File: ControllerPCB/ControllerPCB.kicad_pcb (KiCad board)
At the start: 2 copper layers, 88 parts, among them J1 2x20 Conn_1, J10 Conn_01x03_Pin, J11 1x4 String Output Conn, J12 2x4 Pickup Conn, J13 9V Humbucker OUT, J14 9V IN, J15 MIDI Out Conn, J2 Conn_01x03_Pin, J3 Conn_01x03_Pin, J4 10-pin Debug Conn, J5 Conn_01x03_Pin, J6 Conn_01x03_Pin, J7 USB_B_Micro, J8 2x20 Conn_2, J9 Conn_01x03_Pin, SW1 SW_SPDT, U1 STM32F439ZIT6, U2 ADP3336ARMZ, U3 74LVC1G17, Y1 8MHz

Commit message: rev 0.3
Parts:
- removed D1: D+_TVS, PESD3V6Z1BCSFYL:PMEG3005AESFYL
- removed D10, D11, D12, D13, D14, D15, D16, D17, D6, D7, D8, D9: MBR0520LT, Diode_SMD:D_SOD-123
- removed D2: VBUS_TVS, PESD5V5C1BLYL:PESD5V5C1BLYL
- removed D3: D-_TVS, PESD3V6Z1BCSFYL:PMEG3005AESFYL
- removed D4: TVS_Bat, TPSMB10CA:DIONM5436X244N
- removed J1: 2x20 Conn_1, 75869-107LF:SHDR40W62P254_2X20_5801X920X957P
- removed J10: Conn_01x03_Pin, 22292031:CONN_AE-6410-03A_MOL
- removed J11: 1x4 String Output Conn, 22292041:CONN_AE-6410-04A_MOL
- removed J8: 2x20 Conn_2, 75869-107LF:SHDR40W62P254_2X20_5801X920X957P
- removed R11, R18, R19: 5k, Resistor_SMD:R_0402_1005Metric
- removed R14, R20, R22: 1k, Resistor_SMD:R_0402_1005Metric
- removed R15, R21, R23: 10k, Resistor_SMD:R_0402_1005Metric
- removed R16, R17, R24, R25: 2k, Resistor_SMD:R_0402_1005Metric
- removed SW1: SW_SPDT, JS102011SAQN:SW_JS102011SAQN
- added C401: 10n, Capacitor_SMD:C_0402_1005Metric, F.Cu at (111.2, 137.2)
- added C402: 10n, Capacitor_SMD:C_0402_1005Metric, F.Cu at (117.0, 137.2)
- added C403: 10n, Capacitor_SMD:C_0402_1005Metric, F.Cu at (128.4, 137.2)
- added C404: 10n, Capacitor_SMD:C_0402_1005Metric, F.Cu at (122.7, 137.2)
- added D101: BLUE, LED_SMD:LED_0603_1608Metric, F.Cu at (128.3, 67.2)
- added D102: D_TVS_Small, 0_Footprint_lib:PMEG3005AESFYL, F.Cu at (163.9, 93.3)
- added D103: D_TVS_Small, 0_Footprint_lib:PMEG3005AESFYL, F.Cu at (191.0, 126.3)
- added D104: D_TVS_Small, 0_Footprint_lib:PMEG3005AESFYL, F.Cu at (163.9, 95.2)
- added D105: D_TVS_Small, 0_Footprint_lib:PMEG3005AESFYL, F.Cu at (126.0, 89.3)
- added D106: D_TVS_Small, 0_Footprint_lib:PMEG3005AESFYL, F.Cu at (128.5, 89.3)
- added D107: D_TVS_Small, 0_Footprint_lib:PMEG3005AESFYL, F.Cu at (163.9, 97.3)
- added D108: D_TVS_Small, 0_Footprint_lib:PMEG3005AESFYL, F.Cu at (192.0, 127.4)
- added D109: D_TVS_Small, 0_Footprint_lib:PMEG3005AESFYL, F.Cu at (192.0, 130.3)
- added D110: D_TVS_Small, 0_Footprint_lib:PMEG3005AESFYL, F.Cu at (131.2, 89.3)
- added D111: D_TVS_Small, 0_Footprint_lib:PMEG3005AESFYL, F.Cu at (163.9, 99.3)
- added D112: D_TVS_Small, 0_Footprint_lib:PMEG3005AESFYL, F.Cu at (133.7, 89.3)
- added D113: D_Small, Diode_SMD:D_SOD-323, F.Cu at (134.0, 91.6)
- added D114: D_Small, Diode_SMD:D_SOD-323, F.Cu at (131.5, 91.6)
- added D115: D_Small, Diode_SMD:D_SOD-323, F.Cu at (128.9, 91.6)
- added D116: D_Small, Diode_SMD:D_SOD-323, F.Cu at (126.4, 91.6)
- added D117: D_TVS_Small, 0_Footprint_lib:PMEG3005AESFYL, F.Cu at (169.2, 100.0)
- added D201: D_TVS_Small, 0_Footprint_lib:PMEG3005AESFYL, F.Cu at (151.8, 89.2)
- added D401: D_Small, Diode_SMD:D_SOD-323, F.Cu at (122.2, 132.7)
- added D402: D_Small, Diode_SMD:D_SOD-323, F.Cu at (122.2, 134.7)
- added D403: D_Small, Diode_SMD:D_SOD-323, F.Cu at (110.7, 132.7)
- added D404: D_Small, Diode_SMD:D_SOD-323, F.Cu at (110.7, 134.7)
- added D405: D_Small, Diode_SMD:D_SOD-323, F.Cu at (122.2, 130.7)
- added D406: D_Small, Diode_SMD:D_SOD-323, F.Cu at (110.7, 130.7)
- added D407: D_Small, Diode_SMD:D_SOD-323, F.Cu at (128.0, 132.7)
- added D408: D_Small, Diode_SMD:D_SOD-323, F.Cu at (128.0, 134.7)
- added D409: D_Small, Diode_SMD:D_SOD-323, F.Cu at (116.5, 132.7)
- added D410: D_Small, Diode_SMD:D_SOD-323, F.Cu at (116.5, 134.7)
- added D411: D_Small, Diode_SMD:D_SOD-323, F.Cu at (128.0, 130.7)
- added D412: D_Small, Diode_SMD:D_SOD-323, F.Cu at (116.5, 130.7)
- added D501: D_TVS_Small, 0_Footprint_lib:PMEG3005AESFYL, B.Cu at (193.7, 63.8)
- added D502: D_TVS_Small, 0_Footprint_lib:PMEG3005AESFYL, B.Cu at (193.7, 66.3)
- added D503: D_TVS_Small, 0_Footprint_lib:PMEG3005AESFYL, B.Cu at (193.7, 68.8)
- added D504: D_TVS_Small, 0_Footprint_lib:PMEG3005AESFYL, B.Cu at (193.7, 71.3)
- added D505: D_TVS_Small, 0_Footprint_lib:PMEG3005AESFYL, B.Cu at (193.7, 74.1)
- added D506: D_TVS_Small, 0_Footprint_lib:PMEG3005AESFYL, B.Cu at (193.8, 76.6)
- added D507: D_TVS_Small, 0_Footprint_lib:PMEG3005AESFYL, B.Cu at (193.8, 79.1)
- added D508: D_TVS_Small, 0_Footprint_lib:PMEG3005AESFYL, B.Cu at (193.7, 81.3)
- added D509: D_TVS_Small, 0_Footprint_lib:PMEG3005AESFYL, B.Cu at (193.7, 83.8)
- added D510: D_TVS_Small, 0_Footprint_lib:PMEG3005AESFYL, B.Cu at (193.7, 86.6)
- added D511: D_TVS_Small, 0_Footprint_lib:PMEG3005AESFYL, B.Cu at (193.8, 89.3)
- added D512: D_TVS_Small, 0_Footprint_lib:PMEG3005AESFYL, B.Cu at (193.7, 92.1)
- added D513: D_TVS_Small, 0_Footprint_lib:PMEG3005AESFYL, B.Cu at (193.8, 94.6)
- added D514: D_TVS_Small, 0_Footprint_lib:PMEG3005AESFYL, B.Cu at (193.7, 97.1)
- added D515: D_TVS_Small, 0_Footprint_lib:PMEG3005AESFYL, B.Cu at (193.7, 99.6)
- added D516: D_TVS_Small, 0_Footprint_lib:PMEG3005AESFYL, B.Cu at (193.7, 102.1)
- added D517: D_TVS_Small, 0_Footprint_lib:PMEG3005AESFYL, B.Cu at (193.8, 104.8)
- added D518: D_TVS_Small, 0_Footprint_lib:PMEG3005AESFYL, B.Cu at (193.8, 107.6)
- added D519: D_TVS_Small, 0_Footprint_lib:PMEG3005AESFYL, B.Cu at (193.7, 110.1)
- added D520: D_TVS_Small, 0_Footprint_lib:PMEG3005AESFYL, B.Cu at (193.8, 112.8)
- added D521: D_TVS_Small, 0_Footprint_lib:PMEG3005AESFYL, B.Cu at (181.4, 64.1)
- added D522: D_TVS_Small, 0_Footprint_lib:PMEG3005AESFYL, B.Cu at (181.4, 66.6)
- added D523: D_TVS_Small, 0_Footprint_lib:PMEG3005AESFYL, B.Cu at (181.4, 69.1)
- added D524: D_TVS_Small, 0_Footprint_lib:PMEG3005AESFYL, B.Cu at (181.4, 71.6)
- added D525: D_TVS_Small, 0_Footprint_lib:PMEG3005AESFYL, B.Cu at (181.4, 74.1)
- added D526: D_TVS_Small, 0_Footprint_lib:PMEG3005AESFYL, B.Cu at (181.4, 76.6)
- added D527: D_TVS_Small, 0_Footprint_lib:PMEG3005AESFYL, B.Cu at (181.4, 79.3)
- added D528: D_TVS_Small, 0_Footprint_lib:PMEG3005AESFYL, B.Cu at (181.4, 81.8)
- added D529: D_TVS_Small, 0_Footprint_lib:PMEG3005AESFYL, B.Cu at (181.4, 84.3)
- added D530: D_TVS_Small, 0_Footprint_lib:PMEG3005AESFYL, B.Cu at (181.4, 86.8)
- added D531: D_TVS_Small, 0_Footprint_lib:PMEG3005AESFYL, B.Cu at (181.4, 89.3)
- added D532: D_TVS_Small, 0_Footprint_lib:PMEG3005AESFYL, B.Cu at (181.4, 91.8)
- added D533: D_TVS_Small, 0_Footprint_lib:PMEG3005AESFYL, B.Cu at (181.4, 94.3)
- added D534: D_TVS_Small, 0_Footprint_lib:PMEG3005AESFYL, B.Cu at (181.4, 96.8)
- added D535: D_TVS_Small, 0_Footprint_lib:PMEG3005AESFYL, B.Cu at (181.4, 99.3)
- added D536: D_TVS_Small, 0_Footprint_lib:PMEG3005AESFYL, B.Cu at (181.4, 101.8)
- added D537: D_TVS_Small, 0_Footprint_lib:PMEG3005AESFYL, B.Cu at (181.4, 104.8)
- added D538: D_TVS_Small, 0_Footprint_lib:PMEG3005AESFYL, B.Cu at (181.4, 107.3)
- added D539: D_TVS_Small, 0_Footprint_lib:PMEG3005AESFYL, B.Cu at (181.4, 109.8)
- added D540: D_TVS_Small, 0_Footprint_lib:PMEG3005AESFYL, B.Cu at (181.4, 112.3)
- added D541: D_TVS_Small, 0_Footprint_lib:PMEG3005AESFYL, B.Cu at (94.0, 63.4)
- added D542: D_TVS_Small, 0_Footprint_lib:PMEG3005AESFYL, B.Cu at (106.2, 63.1)
- added D543: D_TVS_Small, 0_Footprint_lib:PMEG3005AESFYL, B.Cu at (94.0, 65.9)
- added D544: D_TVS_Small, 0_Footprint_lib:PMEG3005AESFYL, B.Cu at (106.2, 65.9)
- added D545: D_TVS_Small, 0_Footprint_lib:PMEG3005AESFYL, B.Cu at (94.0, 68.6)
- added D546: D_TVS_Small, 0_Footprint_lib:PMEG3005AESFYL, B.Cu at (106.2, 68.4)
- added D547: D_TVS_Small, 0_Footprint_lib:PMEG3005AESFYL, B.Cu at (94.0, 71.1)
- added D548: D_TVS_Small, 0_Footprint_lib:PMEG3005AESFYL, B.Cu at (106.2, 70.9)
- added D549: D_TVS_Small, 0_Footprint_lib:PMEG3005AESFYL, B.Cu at (94.0, 73.6)
- added D550: D_TVS_Small, 0_Footprint_lib:PMEG3005AESFYL, B.Cu at (106.2, 73.4)
- added D551: D_TVS_Small, 0_Footprint_lib:PMEG3005AESFYL, B.Cu at (94.0, 76.1)
- added D552: D_TVS_Small, 0_Footprint_lib:PMEG3005AESFYL, B.Cu at (106.2, 75.9)
- added D553: D_TVS_Small, 0_Footprint_lib:PMEG3005AESFYL, B.Cu at (94.0, 78.6)
- added D554: D_TVS_Small, 0_Footprint_lib:PMEG3005AESFYL, B.Cu at (106.2, 78.4)
- added D555: D_TVS_Small, 0_Footprint_lib:PMEG3005AESFYL, B.Cu at (94.0, 81.1)
- added D556: D_TVS_Small, 0_Footprint_lib:PMEG3005AESFYL, B.Cu at (106.2, 80.9)
- added D557: D_TVS_Small, 0_Footprint_lib:PMEG3005AESFYL, B.Cu at (94.0, 83.9)
- added D558: D_TVS_Small, 0_Footprint_lib:PMEG3005AESFYL, B.Cu at (106.2, 83.6)
- added D559: D_TVS_Small, 0_Footprint_lib:PMEG3005AESFYL, B.Cu at (94.0, 86.1)
- added D560: D_TVS_Small, 0_Footprint_lib:PMEG3005AESFYL, B.Cu at (106.2, 86.4)
- added D561: D_TVS_Small, 0_Footprint_lib:PMEG3005AESFYL, B.Cu at (94.0, 88.6)
- added D562: D_TVS_Small, 0_Footprint_lib:PMEG3005AESFYL, B.Cu at (106.2, 88.9)
- added D563: D_TVS_Small, 0_Footprint_lib:PMEG3005AESFYL, B.Cu at (94.0, 91.1)
- added D564: D_TVS_Small, 0_Footprint_lib:PMEG3005AESFYL, B.Cu at (106.2, 91.4)
- added D565: D_TVS_Small, 0_Footprint_lib:PMEG3005AESFYL, B.Cu at (94.0, 93.6)
- added D566: D_TVS_Small, 0_Footprint_lib:PMEG3005AESFYL, B.Cu at (106.2, 93.9)
- added D567: D_TVS_Small, 0_Footprint_lib:PMEG3005AESFYL, B.Cu at (94.0, 96.4)
- added D568: D_TVS_Small, 0_Footprint_lib:PMEG3005AESFYL, B.Cu at (106.2, 96.4)
- added D569: D_TVS_Small, 0_Footprint_lib:PMEG3005AESFYL, B.Cu at (94.0, 98.9)
- added D570: D_TVS_Small, 0_Footprint_lib:PMEG3005AESFYL, B.Cu at (106.2, 98.9)
- added D571: D_TVS_Small, 0_Footprint_lib:PMEG3005AESFYL, B.Cu at (94.0, 101.4)
- added D572: D_TVS_Small, 0_Footprint_lib:PMEG3005AESFYL, B.Cu at (106.2, 101.4)
- added D573: D_TVS_Small, 0_Footprint_lib:PMEG3005AESFYL, B.Cu at (94.0, 103.9)
- added D574: D_TVS_Small, 0_Footprint_lib:PMEG3005AESFYL, B.Cu at (106.2, 104.1)
- added D575: D_TVS_Small, 0_Footprint_lib:PMEG3005AESFYL, B.Cu at (94.0, 106.4)
- added D576: D_TVS_Small, 0_Footprint_lib:PMEG3005AESFYL, B.Cu at (106.2, 106.6)
- added D577: D_TVS_Small, 0_Footprint_lib:PMEG3005AESFYL, B.Cu at (94.0, 109.4)
- added D578: D_TVS_Small, 0_Footprint_lib:PMEG3005AESFYL, B.Cu at (106.2, 109.1)
- added D579: D_TVS_Small, 0_Footprint_lib:PMEG3005AESFYL, B.Cu at (94.0, 112.1)
- added D580: D_TVS_Small, 0_Footprint_lib:PMEG3005AESFYL, B.Cu at (106.2, 111.9)
- added H101: MountingHole, MountingHole:MountingHole_3.2mm_M3, F.Cu at (74.0, 59.0)
- added H102: MountingHole, MountingHole:MountingHole_3.2mm_M3, F.Cu at (207.0, 147.0)
- added H103: MountingHole, MountingHole:MountingHole_3.2mm_M3, F.Cu at (207.0, 59.0)
- added H104: MountingHole, MountingHole:MountingHole_3.2mm_M3, F.Cu at (74.0, 147.0)
- added J102: 1x4 String Output Conn, 0_Footprint_lib:CONN_AE-6410-04A_MOL, F.Cu at (133.8, 84.2)
- added J501: 2x20 Conn_1, 0_Footprint_lib:SHDR40W62P254_2X20_5801X920X957P, F.Cu at (189.5, 111.4)
- added J502: 2x20 Conn_2, 0_Footprint_lib:SHDR40W62P254_2X20_5801X920X957P, F.Cu at (101.5, 111.8)
- added R101: 1k, Resistor_SMD:R_0402_1005Metric, F.Cu at (127.8, 69.2)
- added R104: 22R, Resistor_SMD:R_0402_1005Metric, F.Cu at (161.7, 99.3)
- added R105: 22R, Resistor_SMD:R_0402_1005Metric, F.Cu at (161.7, 97.3)
- added R106: 22R, Resistor_SMD:R_0402_1005Metric, F.Cu at (161.7, 95.2)
- added R107: 22R, Resistor_SMD:R_0402_1005Metric, F.Cu at (161.8, 93.3)
- added R401: 1k, Resistor_SMD:R_0402_1005Metric, F.Cu at (121.7, 136.2)
- added R403: 220, Resistor_SMD:R_0402_1005Metric, F.Cu at (124.5, 132.2)
- added R404: 2k, Resistor_SMD:R_0402_1005Metric, F.Cu at (125.5, 133.2)
- added R407: 1k, Resistor_SMD:R_0402_1005Metric, F.Cu at (127.5, 136.2)
- added R408: 220, Resistor_SMD:R_0402_1005Metric, F.Cu at (130.2, 132.2)
- added R409: 2k, Resistor_SMD:R_0402_1005Metric, F.Cu at (131.2, 133.2)
- added R410: 1k, Resistor_SMD:R_0402_1005Metric, F.Cu at (116.0, 136.2)
- added R411: 220, Resistor_SMD:R_0402_1005Metric, F.Cu at (118.7, 132.2)
- added R412: 2k, Resistor_SMD:R_0402_1005Metric, F.Cu at (119.7, 133.2)
- J101: renamed from J12; footprint 75869_332LF:AMPHENOL_75869-332LF -> 0_Footprint_lib:AMPHENOL_75869-332LF
- J103: renamed from J2; footprint 22292031:CONN_AE-6410-03A_MOL -> 0_Footprint_lib:CONN_AE-6410-03A_MOL
- J104: renamed from J3; footprint 22292031:CONN_AE-6410-03A_MOL -> 0_Footprint_lib:CONN_AE-6410-03A_MOL
- J105: renamed from J5; footprint 22292031:CONN_AE-6410-03A_MOL -> 0_Footprint_lib:CONN_AE-6410-03A_MOL
- J106: renamed from J6; footprint 22292031:CONN_AE-6410-03A_MOL -> 0_Footprint_lib:CONN_AE-6410-03A_MOL
- J108: renamed from J4; footprint FTSH_105_01_F_D_K:SAMTEC_FTSH-105-01-F-D-K -> 0_Footprint_lib:SAMTEC_FTSH-105-01-F-D-K
- J109: renamed from J9; footprint 22292031:CONN_AE-6410-03A_MOL -> 0_Footprint_lib:CONN_AE-6410-03A_MOL
- J201: renamed from J13; footprint 3_641126_2:TE_3-641126-2 -> 0_Footprint_lib:TE_3-641126-2
- J202: renamed from J14; footprint PowerConnector:APP_ASMPR45-1X2-RK -> 0_Footprint_lib:APP_ASMPR45-1X2-RK
- J301: renamed from J15; footprint 22292031:CONN_AE-6410-03A_MOL -> 0_Footprint_lib:CONN_AE-6410-03A_MOL
- R402: renamed from R10; value 5k -> 1k
- R405: renamed from R12; value 1k -> 220
- R406: renamed from R13; value 10k -> 2k
- U201: renamed from U2; footprint ADP3336ARMZ_REEL7:RM_8_ADI -> 0_Footprint_lib:RM_8_ADI
- U301: renamed from U3; footprint SN74LVC1G17DBVR:SOT95P280X145-5N -> 0_Footprint_lib:SOT95P280X145-5N
- Y101: renamed from Y1; value 8MHz -> 16MHz; footprint 830059082:830059082 -> Crystal:Crystal_SMD_3225-4Pin_3.2x2.5mm
- moved J103 104.7 mm to (140.3, 137.5), turned to 0 degrees
- moved J105 100.7 mm to (140.3, 144.2), turned to 0 degrees
- moved J104 92.4 mm to (149.8, 137.5), turned to 0 degrees
- moved J109 87.9 mm to (149.8, 144.2), turned to 0 degrees
- moved R102 85.9 mm to (122.5, 96.8)
- moved C104 78.9 mm to (127.8, 127.1)
- moved J106 78.8 mm to (159.3, 137.5), turned to 0 degrees
- moved R103 78.7 mm to (126.5, 101.2)
- moved C102 78.5 mm to (123.2, 108.3)
- moved C105 78.5 mm to (134.7, 127.1)
- moved C107 78.5 mm to (139.7, 127.1)
- moved C109 78.5 mm to (146.7, 125.6)
- moved C110 78.5 mm to (148.7, 118.1)
- moved C111 78.5 mm to (148.7, 112.6)
- moved C114 78.5 mm to (145.0, 127.1)
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- renumbered C1 to C101, C2 to C102, C3 to C103, C4 to C104, C5 to C105, C6 to C106, C7 to C107, C8 to C108, C9 to C109, C10 to C110, C11 to C111, C12 to C112, C13 to C113, C14 to C114, C15 to C115, C16 to C116, C17 to C117, C18 to C118, C19 to C119, C22 to C120, C23 to C121, C24 to C122, C25 to C201, C26 to C202, C27 to C203, D5 to D202, FB1 to FB101, J7 to J107, R2 to R102, R1 to R103, R3 to R108, R4 to R109, R5 to R201, R6 to R202, R7 to R203, R8 to R301, R9 to R302, U1 to U101
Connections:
- net ADC_Mod renamed ADC_Mode
- net ADC_Thresh renamed ADC_Slider
- net Net-(D5-K) renamed /Power/LED_GREEN
- net Net-(R12-Pad2) renamed /Amplitude Detection/3V_OUT_1
- net Net-(U2-FB) renamed /Power/FB_IN
- J108 pad 02: SWDIO -> /CONN_SWDIO
- J108 pad 04: SWDCLK -> /CONN_SWCLK
- J108 pad 06: SWO -> /CONN_SWO
- J108 pad 10: NRST -> /CONN_NRST
- R102 pad 1: /SW_BOOT0 -> GND
- R402 pad 2: Net-(D10-A) -> /Amplitude Detection/ADC_Diode_Net_1
- U101 pad 132: unconnected-(U1-PG15-Pad132) -> /LED_OUT
- U101 pad 47: ADC_Extra -> unconnected-(U101-PB1-Pad47)
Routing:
- net GND: track 0.00 -> 83.8 mm, vias 0 -> 30
- net D-: track 0.00 -> 55.2 mm
- net D+: track 0.00 -> 55.2 mm
- net VBUS_Sense: track 0.00 -> 52.7 mm
- net +3.3V: track 0.00 -> 39.9 mm
- net ADC_Slider: track 0.00 -> 30.3 mm
- net ADC_Bend: track 0.00 -> 26.8 mm
- net ADC_Mode: track 0.00 -> 23.4 mm
- net ADC_MIDI_Ch: track 0.00 -> 22.3 mm
- net ADC_String_1_F: track 0.00 -> 18.6 mm
- net ADC_Octave: track 0.00 -> 15.9 mm
- net String_4_out: track 0.00 -> 15.4 mm
- net String_3_out: track 0.00 -> 14.2 mm
- net String_2_out: track 0.00 -> 13.4 mm
- net ADC_String_2: track 0.00 -> 13.0 mm
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- added copper zone on F.Cu, net +3.3V
- added copper zone on F.Cu, net /Power/9V+
- added copper zone on F.Cu, net GND
- added copper zone on In1.Cu, net GND
- added copper zone on In2.Cu, net GND
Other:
- copper layers 2 -> 4

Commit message: rev 0.4
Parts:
- removed C401, C402, C403, C404: 10n, Capacitor_SMD:C_0402_1005Metric
- D501, D502, D503, D504, D505, D506, D507, D508, D509, D510, D511, D512, D513, D514, D515, D516, D517, D518, D519, D520, D521, D522, D523, D524, D525, D526, D527, D528, D529, D530, D531, D532, D533, D534, D535, D536, D537, D538, D539, D540, D541, D542, D543, D544, D545, D546, D547, D548, D549, D550, D551, D552, D553, D554, D555, D556, D557, D558, D559, D560, D561, D562, D563, D564, D565, D566, D567, D568, D569, D570, D571, D572, D573, D574, D575, D576, D577, D578, D579, D580: moved to F.Cu
- moved R101 66.2 mm to (160.5, 126.8), turned to 180 degrees
- moved D101 65.9 mm to (160.6, 124.8)
- moved D102 3.00 mm to (160.9, 93.3)
- moved D104 3.00 mm to (160.9, 95.2)
- moved D107 3.00 mm to (160.9, 97.3)
- moved D111 3.00 mm to (160.9, 99.3)
- moved D117 3.00 mm to (166.2, 100.0)
- moved J108 3.00 mm to (164.6, 96.0)
- moved R104 3.00 mm to (158.7, 99.3)
- moved R105 3.00 mm to (158.7, 97.3)
- moved R106 3.00 mm to (158.7, 95.2)
- moved R107 3.00 mm to (158.8, 93.3)
- moved C102 0.10 mm to (123.2, 108.2)
- moved D541 0.05 mm to (94.0, 63.4), turned to 0 degrees
- moved D543 0.05 mm to (94.0, 65.9), turned to 0 degrees
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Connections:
- J501 pad 1: input_1 -> input_41
- J501 pad 10: input_25 -> input_50
- J501 pad 11: input_6 -> input_51
- J501 pad 12: input_26 -> input_52
- J501 pad 13: input_7 -> input_53
- J501 pad 14: input_27 -> input_54
- J501 pad 15: input_8 -> input_55
- J501 pad 16: input_28 -> input_56
- J501 pad 17: input_9 -> input_57
- J501 pad 18: input_29 -> input_58
- J501 pad 19: input_10 -> input_59
- J501 pad 2: input_21 -> input_42
- J501 pad 20: input_30 -> input_60
- J501 pad 21: input_11 -> input_61
- J501 pad 22: input_31 -> input_62
- J501 pad 23: input_12 -> input_63
- J501 pad 24: input_32 -> input_64
- J501 pad 25: input_13 -> input_65
- J501 pad 26: input_33 -> input_66
- J501 pad 27: input_14 -> input_67
- J501 pad 28: input_34 -> input_68
- J501 pad 29: input_15 -> input_69
- J501 pad 3: input_2 -> input_43
- J501 pad 30: input_35 -> input_70
- J501 pad 31: input_16 -> input_71
- J501 pad 32: input_36 -> input_72
- J501 pad 33: input_17 -> input_73
- J501 pad 34: input_37 -> input_74
- J501 pad 35: input_18 -> input_75
- J501 pad 36: input_38 -> input_76
- J501 pad 37: input_19 -> input_77
- J501 pad 38: input_39 -> input_78
- J501 pad 39: input_20 -> input_79
- J501 pad 4: input_22 -> input_44
- J501 pad 40: input_40 -> input_80
- J501 pad 5: input_3 -> input_45
- J501 pad 6: input_23 -> input_46
- J501 pad 7: input_4 -> input_47
- J501 pad 8: input_24 -> input_48
- J501 pad 9: input_5 -> input_49
- J502 pad 1: input_41 -> input_1
- J502 pad 10: input_65 -> input_10
- J502 pad 11: input_46 -> input_11
- J502 pad 12: input_66 -> input_12
- J502 pad 13: input_47 -> input_13
- J502 pad 14: input_67 -> input_14
- J502 pad 15: input_48 -> input_15
- J502 pad 16: input_68 -> input_16
- J502 pad 17: input_49 -> input_17
- J502 pad 18: input_69 -> input_18
- J502 pad 19: input_50 -> input_19
- J502 pad 2: input_61 -> input_2
- J502 pad 20: input_70 -> input_20
- J502 pad 21: input_51 -> input_21
- J502 pad 22: input_71 -> input_22
- J502 pad 23: input_52 -> input_23
- J502 pad 24: input_72 -> input_24
- J502 pad 25: input_53 -> input_25
- J502 pad 26: input_73 -> input_26
- J502 pad 27: input_54 -> input_27
- J502 pad 28: input_74 -> input_28
- J502 pad 29: input_55 -> input_29
- J502 pad 3: input_42 -> input_3
- J502 pad 30: input_75 -> input_30
- J502 pad 31: input_56 -> input_31
- J502 pad 32: input_76 -> input_32
- J502 pad 33: input_57 -> input_33
- J502 pad 34: input_77 -> input_34
- J502 pad 35: input_58 -> input_35
- J502 pad 36: input_78 -> input_36
- J502 pad 37: input_59 -> input_37
- J502 pad 38: input_79 -> input_38
- J502 pad 39: input_60 -> input_39
- J502 pad 4: input_62 -> input_4
- J502 pad 40: input_80 -> input_40
- J502 pad 5: input_43 -> input_5
- J502 pad 6: input_63 -> input_6
- J502 pad 7: input_44 -> input_7
- J502 pad 8: input_64 -> input_8
- J502 pad 9: input_45 -> input_9
- U101 pad 1: input_40 -> input_10
- U101 pad 10: input_54 -> input_3
- U101 pad 100: input_1 -> input_67
- U101 pad 102: input_2 -> input_70
- U101 pad 11: input_55 -> input_26
- U101 pad 110: input_3 -> input_69
- U101 pad 111: input_19 -> input_72
- U101 pad 112: input_20 -> input_71
- U101 pad 113: input_21 -> input_74
- U101 pad 114: input_25 -> input_73
- U101 pad 115: input_26 -> input_76
- U101 pad 116: input_27 -> input_75
- U101 pad 117: input_28 -> input_78
- U101 pad 118: input_29 -> input_77
- U101 pad 119: input_30 -> input_80
- U101 pad 12: input_56 -> input_4
- U101 pad 122: input_31 -> input_79
- U101 pad 123: input_32 -> input_40
- U101 pad 124: input_79 -> input_39
- U101 pad 129: input_80 -> input_38
- U101 pad 13: input_57 -> input_1
- U101 pad 132: /LED_OUT -> unconnected-(U101-PG15-Pad132)
- U101 pad 134: unconnected-(U101-PB4-Pad134) -> input_37
- U101 pad 135: unconnected-(U101-PB5-Pad135) -> input_36
- U101 pad 136: unconnected-(U101-PB6-Pad136) -> input_35
- U101 pad 137: unconnected-(U101-PB7-Pad137) -> input_34
- U101 pad 139: unconnected-(U101-PB8-Pad139) -> input_32
- U101 pad 14: input_58 -> input_2
- U101 pad 140: unconnected-(U101-PB9-Pad140) -> input_33
- U101 pad 141: unconnected-(U101-PE0-Pad141) -> input_31
- U101 pad 142: unconnected-(U101-PE1-Pad142) -> input_30
- U101 pad 15: input_59 -> input_25
- U101 pad 18: input_60 -> input_24
- U101 pad 19: input_61 -> input_21
- U101 pad 2: input_41 -> input_7
- U101 pad 20: input_62 -> input_23
- U101 pad 21: input_63 -> input_22
- U101 pad 22: input_64 -> input_20
- U101 pad 27: input_10 -> input_19
- U101 pad 28: input_11 -> input_18
- U101 pad 29: input_12 -> input_17
- U101 pad 3: input_42 -> input_8
- U101 pad 4: input_43 -> input_5
- U101 pad 44: input_13 -> input_16
- U101 pad 45: input_14 -> input_15
- U101 pad 49: input_65 -> input_14
- U101 pad 5: input_44 -> input_29
- U101 pad 50: input_66 -> input_13
- U101 pad 53: input_67 -> input_12
- U101 pad 54: input_68 -> input_11
- U101 pad 55: input_69 -> input_42
- U101 pad 56: input_70 -> input_9
- U101 pad 57: input_71 -> input_41
- U101 pad 58: input_45 -> input_44
- U101 pad 59: input_46 -> input_43
- U101 pad 60: input_47 -> input_46
- U101 pad 63: input_48 -> input_45
- U101 pad 64: input_49 -> input_48
- U101 pad 65: input_50 -> input_49
- U101 pad 66: input_51 -> input_47
- U101 pad 68: input_53 -> input_50
- U101 pad 69: input_4 -> input_51
- U101 pad 7: input_22 -> input_28
- U101 pad 70: input_5 -> input_54
- U101 pad 73: input_6 -> input_53
- U101 pad 74: input_7 -> /LED_OUT
- U101 pad 75: input_8 -> input_56
- U101 pad 76: input_9 -> input_55
- U101 pad 78: input_33 -> input_58
- U101 pad 79: input_34 -> unconnected-(U101-PD10-Pad79)
- U101 pad 8: input_23 -> input_27
- U101 pad 80: input_35 -> unconnected-(U101-PD11-Pad80)
- U101 pad 81: input_36 -> unconnected-(U101-PD12-Pad81)
- U101 pad 82: input_37 -> input_57
- U101 pad 85: input_38 -> input_60
- U101 pad 86: input_39 -> input_59
- U101 pad 87: input_72 -> unconnected-(U101-PG2-Pad87)
- U101 pad 88: input_73 -> input_62
- U101 pad 89: input_74 -> unconnected-(U101-PG4-Pad89)
- U101 pad 9: input_24 -> input_6
- U101 pad 90: input_75 -> input_61
- U101 pad 91: input_76 -> unconnected-(U101-PG6-Pad91)
- U101 pad 92: input_77 -> input_64
- U101 pad 93: input_78 -> input_63
- U101 pad 96: input_15 -> input_66
- U101 pad 97: input_16 -> unconnected-(U101-PC7-Pad97)
- U101 pad 98: input_17 -> input_65
- U101 pad 99: input_18 -> input_68
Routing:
- net input_43: track 1.86 -> 91.8 mm
- net input_79: track 6.81 -> 91.5 mm
- net input_77: track 0.00 -> 82.5 mm, vias 0 -> 1
- net input_78: track 0.00 -> 80.8 mm, vias 0 -> 1
- net input_80: track 7.10 -> 86.1 mm
- net input_40: track 2.29 -> 81.1 mm
- net input_75: track 0.00 -> 78.4 mm, vias 0 -> 1
- net input_76: track 0.00 -> 76.6 mm, vias 0 -> 1
- net input_73: track 0.00 -> 75.1 mm, vias 0 -> 1
- net input_38: track 0.00 -> 74.5 mm, vias 0 -> 1
- net input_39: track 0.00 -> 73.6 mm, vias 0 -> 1
- net input_74: track 0.00 -> 72.8 mm, vias 0 -> 1
- net input_71: track 0.00 -> 71.6 mm, vias 0 -> 1
- net input_72: track 0.00 -> 69.1 mm, vias 0 -> 1
- net input_45: track 0.00 -> 68.4 mm, vias 0 -> 1
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
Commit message: rev 1.0
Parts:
- D104, D107, D111, D513, D514, D515, D516, D517, D518, D519, D520, R104, R105, R106: moved to B.Cu
- moved D579 104.1 mm to (194.8, 86.0), turned to -90 degrees
- moved D573 102.9 mm to (194.8, 83.1), turned to 90 degrees
- moved D571 102.8 mm to (194.8, 80.9), turned to -90 degrees
- moved D503 102.8 mm to (93.5, 91.3), turned to -90 degrees
- moved D502 102.7 mm to (93.5, 88.5), turned to 90 degrees
- moved D577 102.5 mm to (193.8, 86.0), turned to -90 degrees
- moved D575 102.4 mm to (193.8, 83.1), turned to 90 degrees
- moved D501 102.3 mm to (94.5, 88.5), turned to 90 degrees
- moved D563 101.9 mm to (194.8, 75.8), turned to -90 degrees
- moved D565 101.9 mm to (194.8, 78.1), turned to 90 degrees
- moved D507 101.7 mm to (93.5, 96.4), turned to -90 degrees
- moved D506 101.7 mm to (93.5, 93.6), turned to 90 degrees
- moved D567 101.5 mm to (193.8, 78.1), turned to 90 degrees
- moved D569 101.4 mm to (193.8, 80.9), turned to -90 degrees
- moved D557 101.4 mm to (194.8, 73.2), turned to 90 degrees
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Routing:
- net +3.3V: track 39.9 -> 458.8 mm, vias 0 -> 11
- net GND: track 74.8 -> 185.1 mm, vias 30 -> 680
- net input_5: track 0.00 -> 32.6 mm
- net input_43: track 91.8 -> 71.9 mm
- net input_68: track 56.0 -> 66.8 mm
- net input_70: track 59.0 -> 69.8 mm
- net input_64: track 57.9 -> 68.0 mm
- net input_66: track 58.4 -> 68.2 mm
- net input_1: track 24.5 -> 33.9 mm
- net input_23: track 45.9 -> 55.0 mm
- net input_62: track 57.5 -> 66.5 mm
- net input_3: track 24.5 -> 33.4 mm
- net input_50: track 60.2 -> 69.0 mm
- net input_39: track 73.6 -> 82.4 mm
- net input_27: track 45.8 -> 54.5 mm
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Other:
- board outline added: 124.5 x 91.5 mm

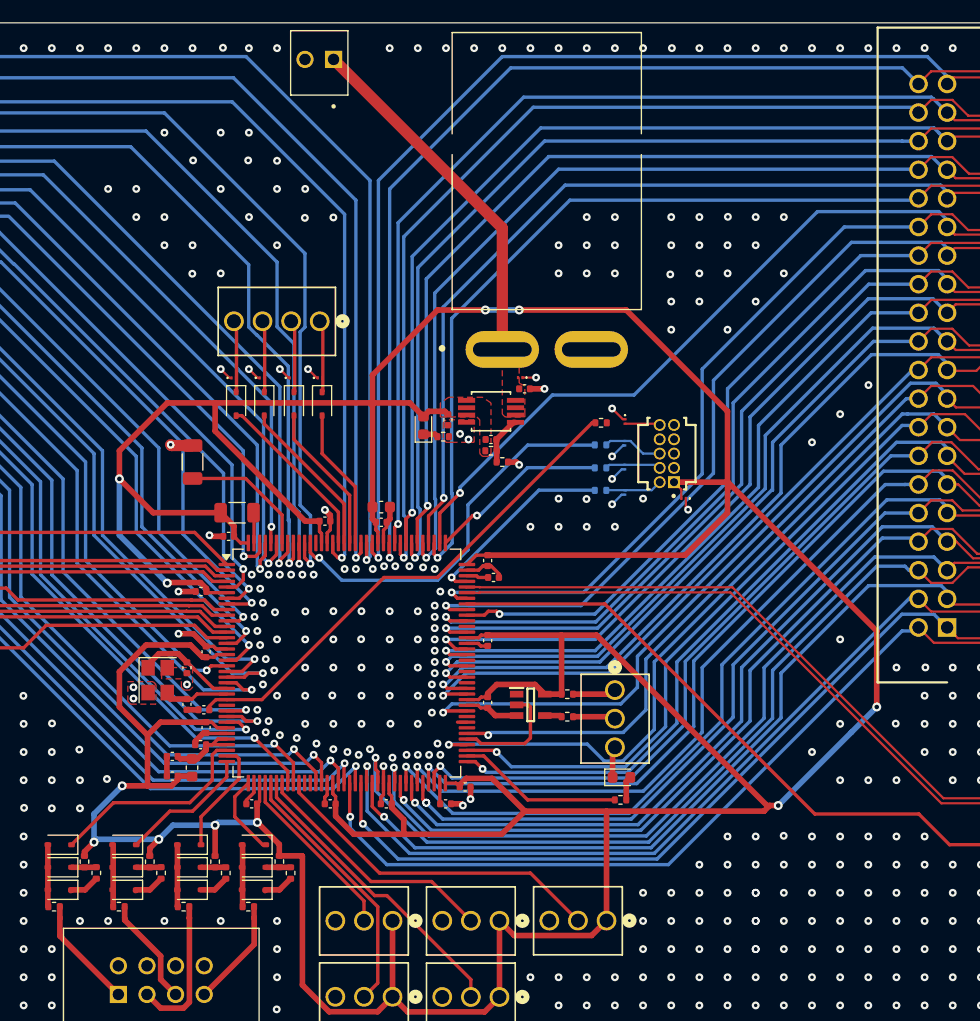
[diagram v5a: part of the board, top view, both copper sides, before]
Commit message: rev 1.01 added "manufacturing" folder - keep the gerber and manufacturing files in here
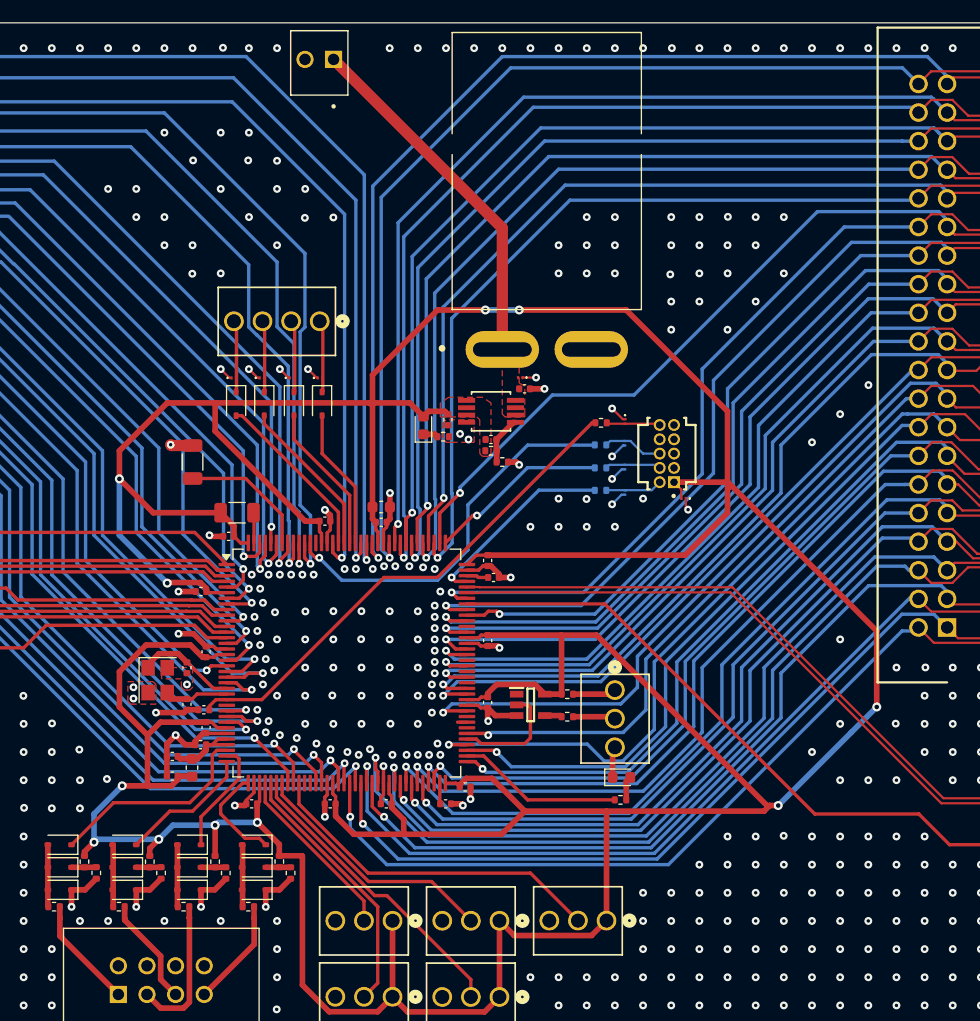
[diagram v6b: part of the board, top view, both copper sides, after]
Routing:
- net GND: track 185.1 -> 204.8 mm, vias 680 -> 689
- net ADC_String_4_F: track 7.26 -> 9.18 mm
- net /CONN_NRST: track 3.13 -> 4.78 mm
- net input_80: track 94.6 -> 95.2 mm
- net input_64: track 68.0 -> 68.7 mm
- net ADC_Slider: track 30.3 -> 30.9 mm
- net input_50: vias 2 -> 1

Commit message: rev1.02
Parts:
- added G***: LOGO, LOGO, F.Cu at (174.8, 106.8)
- added G***: LOGO, LOGO, B.Cu at (114.2, 86.5)
- moved D108 0.10 mm to (198.1, 127.5)
- moved D103 0.08 mm to (197.1, 126.2)
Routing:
- net GND: vias 689 -> 684
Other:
- board text added: "9V OUT"
- board text added: "MIDI CONTROL INPUTS"
- board text added: "MIDI OUT"
- board text added: "PICKUP IN"
- board text added: "STRING OUT"
- board text added: "SWD"
- board text added: "Thog."
- board text added: "USB"

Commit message: rev 1.04
- gerbers/BOM/CPL files are all generated.
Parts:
- C108, C112: value 10p -> 12p
- C114, C117: footprint Capacitor_SMD:C_0402_1005Metric -> Capacitor_SMD:C_0603_1608Metric
- D109: value D_TVS_Small -> D_TVS_VBUS
- moved C113 0.65 mm to (148.9, 104.9)
- moved C114 0.56 mm to (145.5, 127.1)
- moved C117 0.54 mm to (149.8, 106.9)
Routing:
- net GND: track 204.8 -> 205.3 mm, vias 684 -> 685
